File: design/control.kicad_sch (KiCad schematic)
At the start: 1 part, among them U1 STM32F303RETx

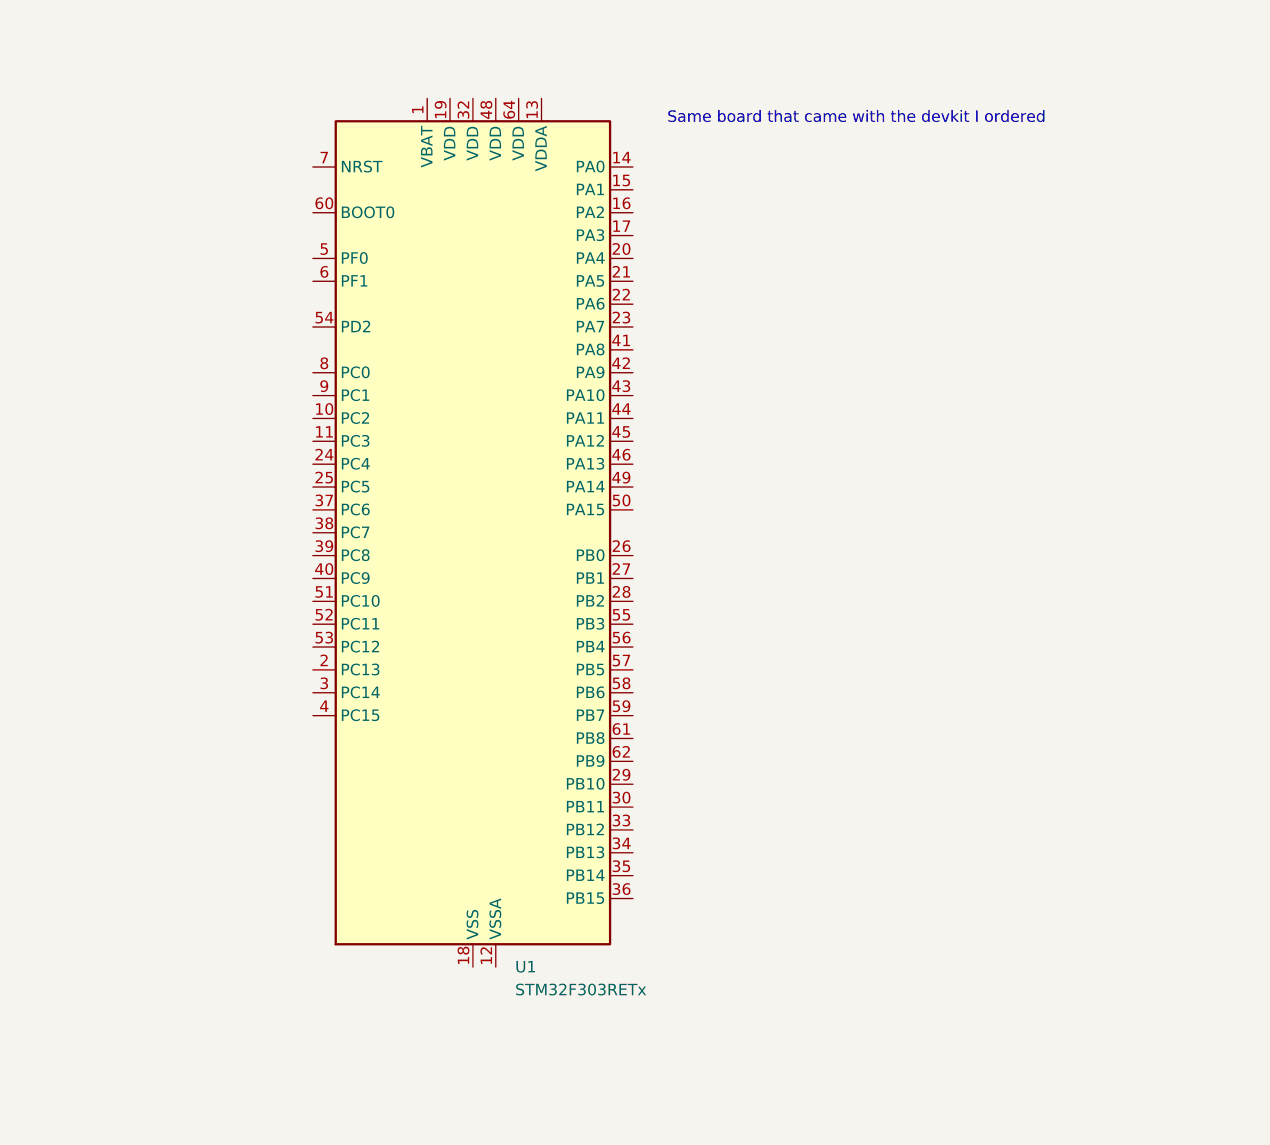
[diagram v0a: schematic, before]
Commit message: started microcontroller setup
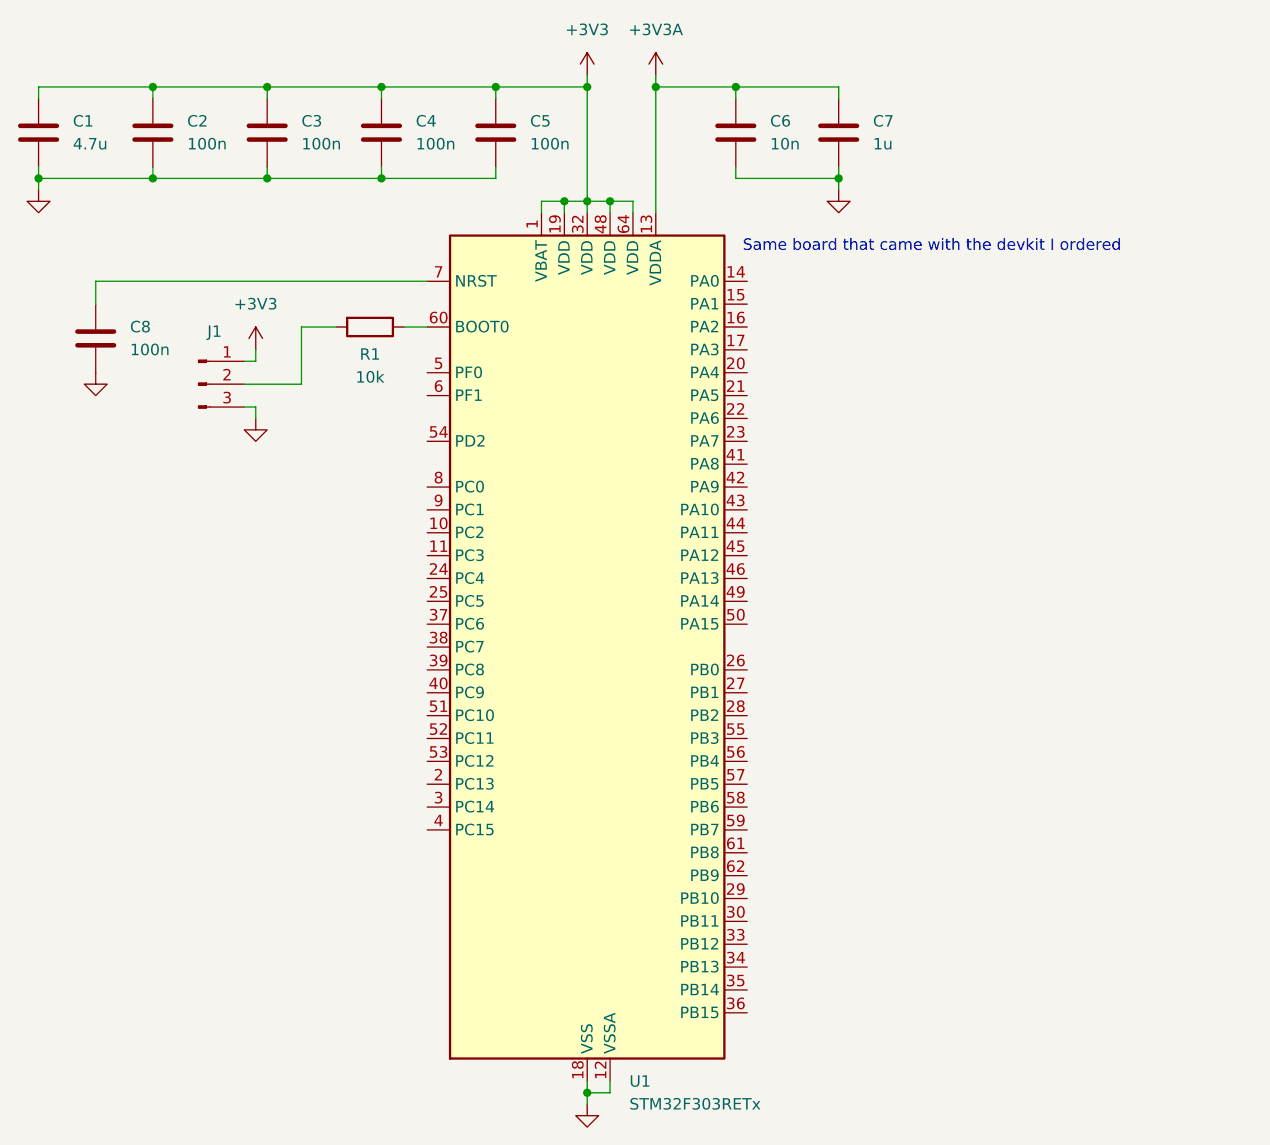
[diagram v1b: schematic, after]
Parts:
- added C1: 4.7u, symbol Device:C
- added C2, C3, C4, C5, C8: 100n, symbol Device:C
- added C6: 10n, symbol Device:C
- added C7: 1u, symbol Device:C
- added J1: Conn_01x03_Pin, symbol Connector:Conn_01x03_Pin
- added R1: 10k, symbol Device:R
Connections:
- net +3V3: now reaches U1.1 (VBAT)
- net +3V3: now also U1.19 (VDD), U1.32 (VDD), U1.48 (VDD), U1.64 (VDD), C1.1, C2.1, C3.1, C4.1, C5.1, J1.1 (Pin_1)
- net GND: now reaches U1.12 (VSSA)
- net GND: now also U1.18 (VSS), U1.31 (VSS), U1.47 (VSS), U1.63 (VSS), C1.2, C2.2, C3.2, C4.2, C5.2, C6.2, C7.2, C8.2, J1.3 (Pin_3)
- net +3V3A: now reaches U1.13 (VDDA)
- net +3V3A: now also C6.1, C7.1
- net at U1.60 (BOOT0): now also R1.1
- net at U1.7 (NRST): now also C8.1
- new net: J1.2 (Pin_2), R1.2
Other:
- moved on the sheet: U1

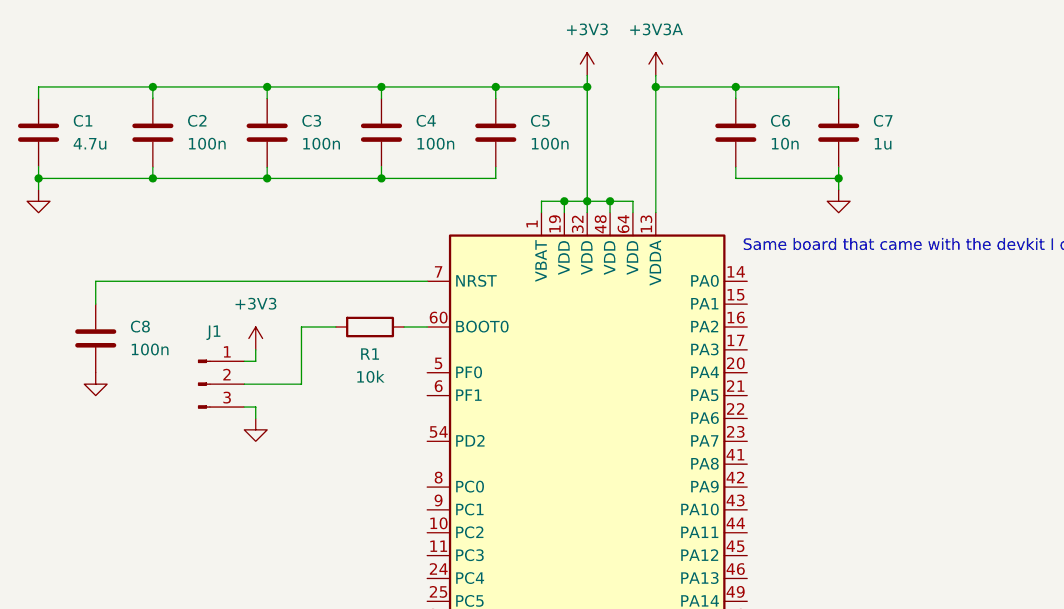
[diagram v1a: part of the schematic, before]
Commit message: started primary power distribution design
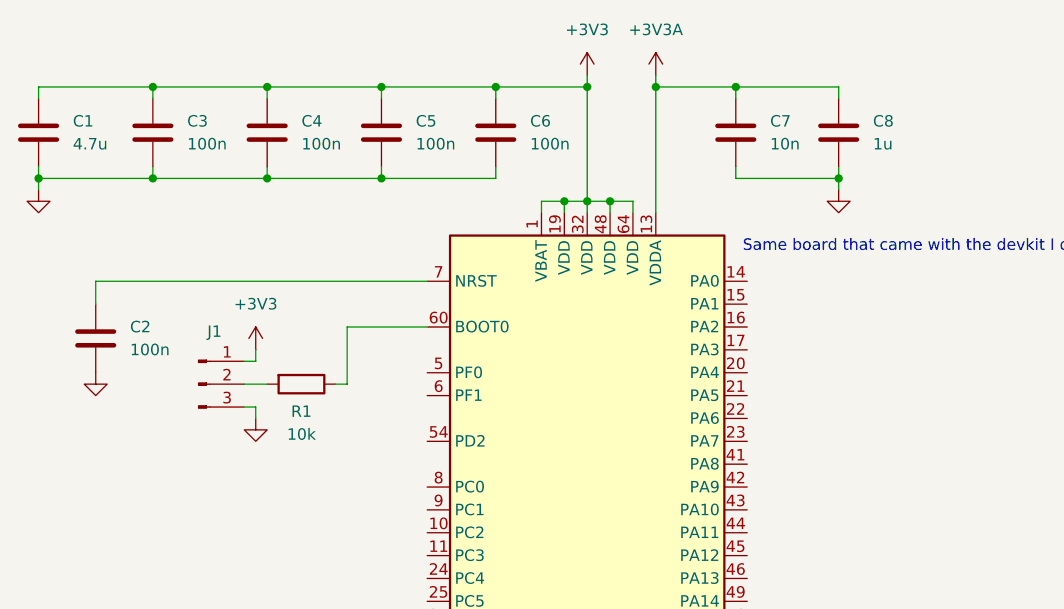
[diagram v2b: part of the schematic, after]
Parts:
- renumbered C8 to C2, C2 to C3, C3 to C4, C4 to C5, C5 to C6, C6 to C7, C7 to C8
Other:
- company: (none) -> UNH Resilient Architecture Lab
- title: (none) -> BitCrusher: Affordable, Open Source EMFI Platform
- moved on the sheet: R1
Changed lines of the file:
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@@
 	(generator_version "9.0")
 	(paper "A4")
+	(title_block
+		(title "BitCrusher: Affordable, Open Source EMFI Platform")
+		(rev "0.1")
+		(company "UNH Resilient Architecture Lab")
+		(comment 1 "Author: George Crane")
+	)
 	(text "Same board that came with the devkit I ordered"
 		(exclude_from_sim no)
@@
 	(wire
 		(pts
-			(xy 41.91 68.58) (xy 48.26 68.58)
+			(xy 41.91 68.58) (xy 44.45 68.58)
 		)
 		(stroke
@@
 	(wire
 		(pts
+			(xy 53.34 62.23) (xy 62.23 62.23)
+		)
+		(stroke
+			(width 0)
+			(type default)
+		)
+	)
+	(wire
+		(pts
 			(xy 41.91 66.04) (xy 43.18 66.04)
 		)
@@
 	(wire
 		(pts
-			(xy 59.69 62.23) (xy 62.23 62.23)
+			(xy 52.07 68.58) (xy 53.34 68.58)
 		)
 		(stroke
@@
 	(wire
 		(pts
-			(xy 48.26 68.58) (xy 48.26 62.23)
+			(xy 53.34 68.58) (xy 53.34 62.23)
 		)
 		(stroke
@@
 		(pts
 			(xy 80.01 48.26) (xy 80.01 49.53)
-		)
-		(stroke
-			(width 0)
-			(type default)
-		)
-	)
-	(wire
-		(pts
-			(xy 48.26 62.23) (xy 52.07 62.23)
 		)
 		(stroke
@@
 		(dnp no)
 		(fields_autoplaced yes)
-		(property "Reference" "C6"
+		(property "Reference" "C7"
 			(at 100.33 39.3699 0)
 			(effects
@@
 			(project ""
 				(path "/e1be550d-9ce6-42b1-a89a-c00b9d7586dd/29f45a98-1f25-4a6e-8231-3aa3a650ea17"
-					(reference "C6")
+					(reference "C7")
 					(unit 1)
 				)
@@
 		(dnp no)
 		(fields_autoplaced yes)
-		(property "Reference" "#PWR02"
+		(property "Reference" "#PWR06"
 			(at 80.01 154.94 0)
 			(effects
@@
 			(project ""
 				(path "/e1be550d-9ce6-42b1-a89a-c00b9d7586dd/29f45a98-1f25-4a6e-8231-3aa3a650ea17"
-					(reference "#PWR02")
+					(reference "#PWR06")
 					(unit 1)
 				)
@@
 		(dnp no)
 		(fields_autoplaced yes)
-		(property "Reference" "#PWR03"
+		(property "Reference" "#PWR01"
 			(at 19.05 53.34 0)
 			(effects
@@
 			(project "BitCrusher"
 				(path "/e1be550d-9ce6-42b1-a89a-c00b9d7586dd/29f45a98-1f25-4a6e-8231-3aa3a650ea17"
-					(reference "#PWR03")
+					(reference "#PWR01")
 					(unit 1)
 				)
@@
 		(dnp no)
 		(fields_autoplaced yes)
-		(property "Reference" "#PWR05"
+		(property "Reference" "#PWR07"
 			(at 87.63 38.1 0)
 			(effects
@@
 			(project ""
 				(path "/e1be550d-9ce6-42b1-a89a-c00b9d7586dd/29f45a98-1f25-4a6e-8231-3aa3a650ea17"
-					(reference "#PWR05")
+					(reference "#PWR07")
 					(unit 1)
 				)
@@
 		(dnp no)
 		(fields_autoplaced yes)
-		(property "Reference" "C2"
+		(property "Reference" "C3"
 			(at 35.56 39.3699 0)
 			(effects
@@
 			(project "BitCrusher"
 				(path "/e1be550d-9ce6-42b1-a89a-c00b9d7586dd/29f45a98-1f25-4a6e-8231-3aa3a650ea17"
-					(reference "C2")
+					(reference "C3")
 					(unit 1)
 				)
@@
 	(symbol
 		(lib_id "Device:R")
-		(at 55.88 62.23 270)
+		(at 48.26 68.58 270)
 		(unit 1)
 		(exclude_from_sim no)
@@
 		(dnp no)
 		(property "Reference" "R1"
-			(at 55.88 65.278 90)
+			(at 48.26 71.628 90)
 			(effects
 				(font
@@
 		)
 		(property "Value" "10k"
-			(at 55.88 67.818 90)
+			(at 48.26 74.168 90)
 			(effects
 				(font
@@
 		)
 		(property "Footprint" ""
-			(at 55.88 60.452 90)
+			(at 48.26 66.802 90)
 			(effects
 				(font
@@
 		)
 		(property "Datasheet" "~"
-			(at 55.88 62.23 0)
+			(at 48.26 68.58 0)
 			(effects
 				(font
@@
 		)
 		(property "Description" "Resistor"
-			(at 55.88 62.23 0)
+			(at 48.26 68.58 0)
 			(effects
 				(font
@@
 		(dnp no)
 		(fields_autoplaced yes)
-		(property "Reference" "#PWR08"
+		(property "Reference" "#PWR03"
 			(at 43.18 68.58 0)
 			(effects
@@
 			(project "BitCrusher"
 				(path "/e1be550d-9ce6-42b1-a89a-c00b9d7586dd/29f45a98-1f25-4a6e-8231-3aa3a650ea17"
-					(reference "#PWR08")
+					(reference "#PWR03")
 					(unit 1)
 				)
@@
 		(dnp no)
 		(fields_autoplaced yes)
-		(property "Reference" "#PWR07"
+		(property "Reference" "#PWR04"
 			(at 43.18 78.74 0)
 			(effects
@@
 			(project "BitCrusher"
 				(path "/e1be550d-9ce6-42b1-a89a-c00b9d7586dd/29f45a98-1f25-4a6e-8231-3aa3a650ea17"
-					(reference "#PWR07")
+					(reference "#PWR04")
 					(unit 1)
 				)
@@
 		(dnp no)
 		(fields_autoplaced yes)
-		(property "Reference" "#PWR01"
+		(property "Reference" "#PWR02"
 			(at 25.4 73.66 0)
 			(effects
@@
 			(project "BitCrusher"
 				(path "/e1be550d-9ce6-42b1-a89a-c00b9d7586dd/29f45a98-1f25-4a6e-8231-3aa3a650ea17"
-					(reference "#PWR01")
+					(reference "#PWR02")
 					(unit 1)
 				)
@@
 		(dnp no)
 		(fields_autoplaced yes)
-		(property "Reference" "C5"
+		(property "Reference" "C6"
 			(at 73.66 39.3699 0)
 			(effects
@@
 			(project "BitCrusher"
 				(path "/e1be550d-9ce6-42b1-a89a-c00b9d7586dd/29f45a98-1f25-4a6e-8231-3aa3a650ea17"
-					(reference "C5")
+					(reference "C6")
 					(unit 1)
 				)
@@
 		(dnp no)
 		(fields_autoplaced yes)
-		(property "Reference" "#PWR04"
+		(property "Reference" "#PWR05"
 			(at 80.01 38.1 0)
 			(effects
@@
 			(project ""
 				(path "/e1be550d-9ce6-42b1-a89a-c00b9d7586dd/29f45a98-1f25-4a6e-8231-3aa3a650ea17"
-					(reference "#PWR04")
+					(reference "#PWR05")
 					(unit 1)
 				)
@@
 		(dnp no)
 		(fields_autoplaced yes)
-		(property "Reference" "#PWR06"
+		(property "Reference" "#PWR08"
 			(at 107.95 53.34 0)
 			(effects
@@
 			(project "BitCrusher"
 				(path "/e1be550d-9ce6-42b1-a89a-c00b9d7586dd/29f45a98-1f25-4a6e-8231-3aa3a650ea17"
-					(reference "#PWR06")
+					(reference "#PWR08")
 					(unit 1)
 				)
@@
 		(dnp no)
 		(fields_autoplaced yes)
-		(property "Reference" "C8"
+		(property "Reference" "C2"
 			(at 29.21 62.2299 0)
 			(effects
@@
 			(project "BitCrusher"
 				(path "/e1be550d-9ce6-42b1-a89a-c00b9d7586dd/29f45a98-1f25-4a6e-8231-3aa3a650ea17"
-					(reference "C8")
+					(reference "C2")
 					(unit 1)
 				)
@@
 		(dnp no)
 		(fields_autoplaced yes)
-		(property "Reference" "C3"
+		(property "Reference" "C4"
 			(at 48.26 39.3699 0)
 			(effects
@@
 			(project "BitCrusher"
 				(path "/e1be550d-9ce6-42b1-a89a-c00b9d7586dd/29f45a98-1f25-4a6e-8231-3aa3a650ea17"
-					(reference "C3")
+					(reference "C4")
 					(unit 1)
 				)
@@
 		(dnp no)
 		(fields_autoplaced yes)
-		(property "Reference" "C4"
+		(property "Reference" "C5"
 			(at 60.96 39.3699 0)
 			(effects
@@
 			(project "BitCrusher"
 				(path "/e1be550d-9ce6-42b1-a89a-c00b9d7586dd/29f45a98-1f25-4a6e-8231-3aa3a650ea17"
-					(reference "C4")
+					(reference "C5")
 					(unit 1)
 				)
@@
 		(dnp no)
 		(fields_autoplaced yes)
-		(property "Reference" "C7"
+		(property "Reference" "C8"
 			(at 111.76 39.3699 0)
 			(effects
@@
 			(project "BitCrusher"
 				(path "/e1be550d-9ce6-42b1-a89a-c00b9d7586dd/29f45a98-1f25-4a6e-8231-3aa3a650ea17"
-					(reference "C7")
+					(reference "C8")
 					(unit 1)
 				)
